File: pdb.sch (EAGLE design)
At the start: 38 parts, among them Q1 20MHz, Q2 IRFR5305PBF, Q3 IRFR5305PBF, U1 TSR_1-2433, U2 LTC2946CMSPBF, U3 LTC2946CMSPBF, U4 LTC2946CMSPBF, U5 ATMEGA48-20AU, U6 TXB0104, U7 AT30TS74SS8M

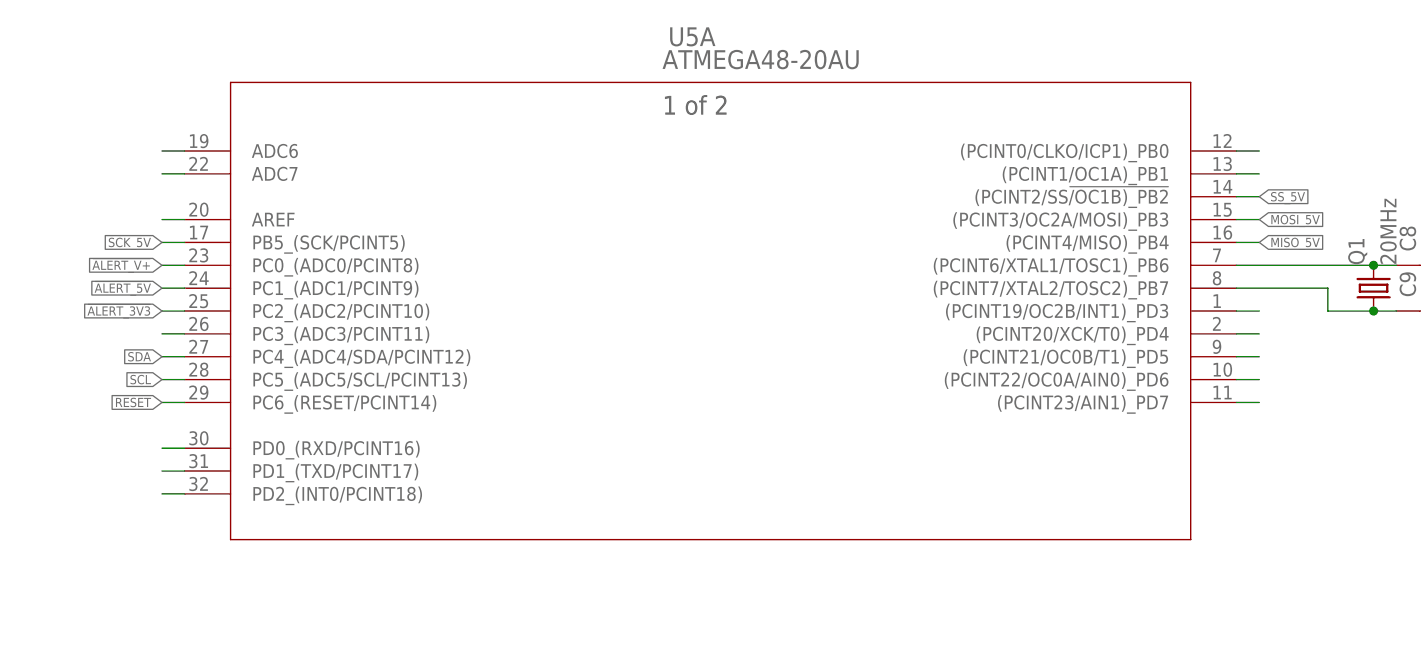
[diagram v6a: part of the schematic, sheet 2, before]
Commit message: 5v nearly completely connected
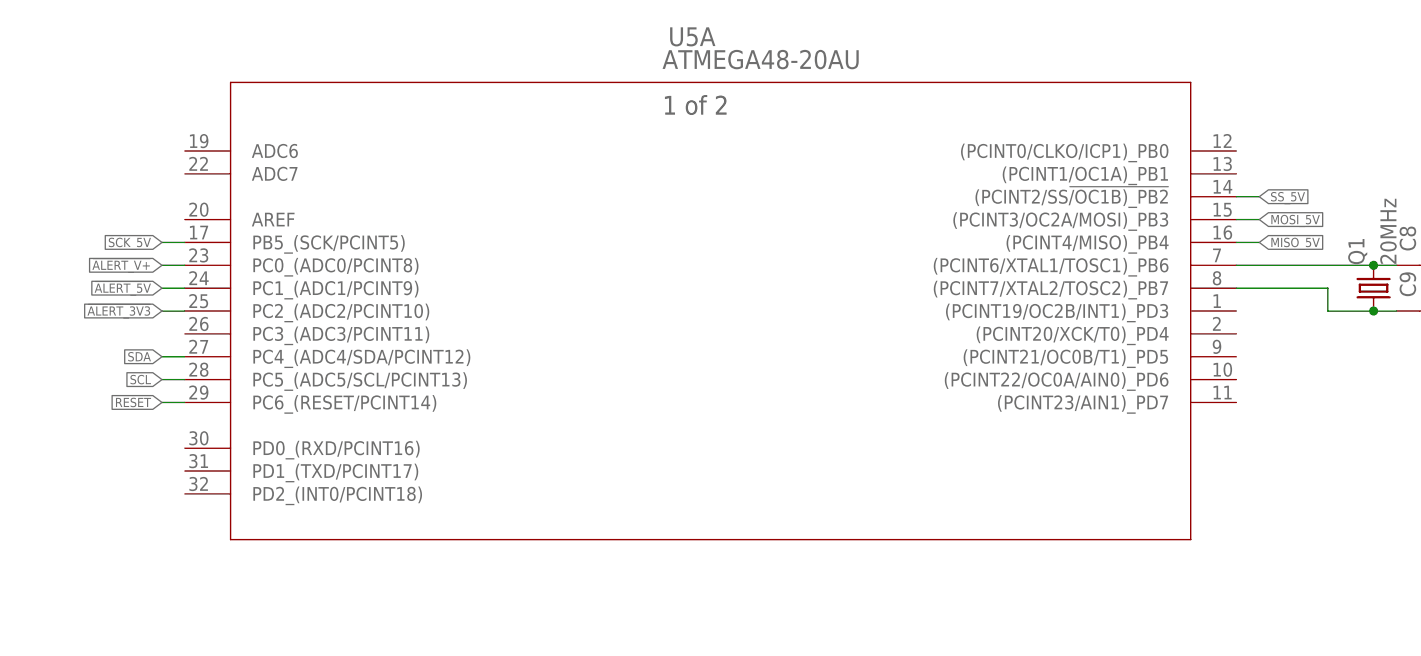
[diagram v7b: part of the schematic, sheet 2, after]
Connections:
- removed net ADIN_3V3: U4.ADIN
- removed net ADIN_5V: U3.ADIN
- removed net ADIN_V+: U2.ADIN
- removed net CLKIN_3V3: U4.CLKIN
- removed net CLKIN_5V: U3.CLKIN
- removed net CLKIN_V+: U2.CLKIN
- removed net CLKOUT_3V3: U4.CLKOUT
- removed net CLKOUT_5V: U3.CLKOUT
- removed net CLKOUT_V+: U2.CLKOUT
- removed net N$10: U5A.AREF
- removed net N$11: U7.ALERT
- removed net N$13: U7.A2
- removed net N$14: U7.A1
- removed net N$15: U5A.PC3_(ADC3/PCINT11)
- removed net N$16: U7.A0
- removed net N$19: U5A.PD0_(RXD/PCINT16)
- removed net N$20: U5A.PD1_(TXD/PCINT17)
- removed net N$21: U5A.PD2_(INT0/PCINT18)
- removed net N$22: U5A.(PCINT0/CLKO/ICP1)_PB0
- removed net N$23: U5A.(PCINT1/OC1A)_PB1
- removed net N$29: U5A.(PCINT19/OC2B/INT1)_PD3
- removed net N$30: U5A.(PCINT20/XCK/T0)_PD4
- removed net N$31: U5A.(PCINT21/OC0B/T1)_PD5
- removed net N$32: U5A.(PCINT22/OC0A/AIN0)_PD6
- removed net N$33: U5A.(PCINT23/AIN1)_PD7
- removed net N$8: U5A.ADC6
- removed net N$9: U5A.ADC7
- removed net SCL_5V: U7.SCL
- removed net SDA_5V: U7.SDA
- net N$88: now also U5B.AVCC
- net SCL: now also U7.SCL
- net SDA: now also U7.SDA
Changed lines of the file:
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@@
 <clearance class="0" value="0.106"/>
 </class>
-<class number="2" name="+14V" width="1.27" drill="0">
+<class number="2" name="V+" width="1.27" drill="0">
 <clearance class="0" value="0.254"/>
 <clearance class="1" value="0.254"/>
 </class>
-<class number="3" name="GND" width="0.4064" drill="0">
+<class number="3" name="GND" width="0.254" drill="0">
 <clearance class="2" value="0.254"/>
 </class>
@@
 </segment>
 </net>
-<net name="N$8" class="0">
-<segment>
-<pinref part="U5" gate="A" pin="ADC6"/>
-<wire x1="83.82" y1="160.02" x2="81.28" y2="160.02" width="0.1524" layer="91"/>
-</segment>
-</net>
-<net name="N$9" class="0">
-<segment>
-<pinref part="U5" gate="A" pin="ADC7"/>
-<wire x1="83.82" y1="157.48" x2="81.28" y2="157.48" width="0.1524" layer="91"/>
-</segment>
-</net>
-<net name="N$10" class="0">
-<segment>
-<pinref part="U5" gate="A" pin="AREF"/>
-<wire x1="83.82" y1="152.4" x2="81.28" y2="152.4" width="0.1524" layer="91"/>
-</segment>
-</net>
 <net name="SCK_5V" class="0">
 <segment>
@@
 </segment>
 </net>
-<net name="N$15" class="0">
-<segment>
-<pinref part="U5" gate="A" pin="PC3_(ADC3/PCINT11)"/>
-<wire x1="83.82" y1="139.7" x2="81.28" y2="139.7" width="0.1524" layer="91"/>
-</segment>
-</net>
 <net name="SDA" class="0">
 <segment>
@@
 <wire x1="83.82" y1="132.08" x2="81.28" y2="132.08" width="0.1524" layer="91"/>
 <label x="81.28" y="132.08" size="1.016" layer="95" rot="R180" xref="yes"/>
-</segment>
-</net>
-<net name="N$19" class="0">
-<segment>
-<pinref part="U5" gate="A" pin="PD0_(RXD/PCINT16)"/>
-<wire x1="83.82" y1="127" x2="81.28" y2="127" width="0.1524" layer="91"/>
-</segment>
-</net>
-<net name="N$20" class="0">
-<segment>
-<pinref part="U5" gate="A" pin="PD1_(TXD/PCINT17)"/>
-<wire x1="83.82" y1="124.46" x2="81.28" y2="124.46" width="0.1524" layer="91"/>
-</segment>
-</net>
-<net name="N$21" class="0">
-<segment>
-<pinref part="U5" gate="A" pin="PD2_(INT0/PCINT18)"/>
-<wire x1="83.82" y1="121.92" x2="81.28" y2="121.92" width="0.1524" layer="91"/>
-</segment>
-</net>
-<net name="N$22" class="0">
-<segment>
-<pinref part="U5" gate="A" pin="(PCINT0/CLKO/ICP1)_PB0"/>
-<wire x1="200.66" y1="160.02" x2="203.2" y2="160.02" width="0.1524" layer="91"/>
-</segment>
-</net>
-<net name="N$23" class="0">
-<segment>
-<pinref part="U5" gate="A" pin="(PCINT1/OC1A)_PB1"/>
-<wire x1="200.66" y1="157.48" x2="203.2" y2="157.48" width="0.1524" layer="91"/>
 </segment>
 </net>
@@
 </segment>
 </net>
-<net name="N$29" class="0">
-<segment>
-<pinref part="U5" gate="A" pin="(PCINT19/OC2B/INT1)_PD3"/>
-<wire x1="200.66" y1="142.24" x2="203.2" y2="142.24" width="0.1524" layer="91"/>
-</segment>
-</net>
-<net name="N$30" class="0">
-<segment>
-<pinref part="U5" gate="A" pin="(PCINT20/XCK/T0)_PD4"/>
-<wire x1="200.66" y1="139.7" x2="203.2" y2="139.7" width="0.1524" layer="91"/>
-</segment>
-</net>
-<net name="N$31" class="0">
-<segment>
-<pinref part="U5" gate="A" pin="(PCINT21/OC0B/T1)_PD5"/>
-<wire x1="200.66" y1="137.16" x2="203.2" y2="137.16" width="0.1524" layer="91"/>
-</segment>
-</net>
-<net name="N$32" class="0">
-<segment>
-<pinref part="U5" gate="A" pin="(PCINT22/OC0A/AIN0)_PD6"/>
-<wire x1="200.66" y1="134.62" x2="203.2" y2="134.62" width="0.1524" layer="91"/>
-</segment>
-</net>
-<net name="N$33" class="0">
-<segment>
-<pinref part="U5" gate="A" pin="(PCINT23/AIN1)_PD7"/>
-<wire x1="200.66" y1="132.08" x2="203.2" y2="132.08" width="0.1524" layer="91"/>
-</segment>
-</net>
 <net name="N$88" class="0">
 <segment>
@@
 <wire x1="106.68" y1="55.88" x2="106.68" y2="50.8" width="0.1524" layer="91"/>
 <junction x="93.98" y="55.88"/>
+<pinref part="U5" gate="B" pin="AVCC"/>
 </segment>
 </net>
@@
 </segment>
 </net>
-<net name="CLKIN_V+" class="0">
-<segment>
-<pinref part="U2" gate="A" pin="CLKIN"/>
-<wire x1="38.1" y1="86.36" x2="35.56" y2="86.36" width="0.1524" layer="91"/>
-</segment>
-</net>
-<net name="ADIN_V+" class="0">
-<segment>
-<pinref part="U2" gate="A" pin="ADIN"/>
-<wire x1="38.1" y1="99.06" x2="35.56" y2="99.06" width="0.1524" layer="91"/>
-</segment>
-</net>
 <net name="INTVCC_V+" class="0">
 <segment>
@@
 </segment>
 </net>
-<net name="CLKOUT_V+" class="0">
-<segment>
-<pinref part="U2" gate="A" pin="CLKOUT"/>
-<wire x1="83.82" y1="99.06" x2="86.36" y2="99.06" width="0.1524" layer="91"/>
-</segment>
-</net>
 <net name="GPIO1_V+" class="0">
 <segment>
@@
 <wire x1="134.62" y1="76.2" x2="132.08" y2="76.2" width="0.1524" layer="91"/>
 <label x="132.08" y="76.2" size="1.016" layer="95" rot="R180" xref="yes"/>
-</segment>
-</net>
-<net name="CLKIN_5V" class="0">
-<segment>
-<pinref part="U3" gate="A" pin="CLKIN"/>
-<wire x1="134.62" y1="86.36" x2="132.08" y2="86.36" width="0.1524" layer="91"/>
-</segment>
-</net>
-<net name="ADIN_5V" class="0">
-<segment>
-<pinref part="U3" gate="A" pin="ADIN"/>
-<wire x1="134.62" y1="99.06" x2="132.08" y2="99.06" width="0.1524" layer="91"/>
-</segment>
-</net>
-<net name="CLKOUT_5V" class="0">
-<segment>
-<pinref part="U3" gate="A" pin="CLKOUT"/>
-<wire x1="180.34" y1="99.06" x2="182.88" y2="99.06" width="0.1524" layer="91"/>
 </segment>
 </net>
@@
 <wire x1="251.46" y1="76.2" x2="248.92" y2="76.2" width="0.1524" layer="91"/>
 <label x="248.92" y="76.2" size="1.016" layer="95" rot="R180" xref="yes"/>
-</segment>
-</net>
-<net name="CLKIN_3V3" class="0">
-<segment>
-<pinref part="U4" gate="A" pin="CLKIN"/>
-<wire x1="251.46" y1="86.36" x2="248.92" y2="86.36" width="0.1524" layer="91"/>
-</segment>
-</net>
-<net name="ADIN_3V3" class="0">
-<segment>
-<pinref part="U4" gate="A" pin="ADIN"/>
-<wire x1="251.46" y1="99.06" x2="248.92" y2="99.06" width="0.1524" layer="91"/>
-</segment>
-</net>
-<net name="CLKOUT_3V3" class="0">
-<segment>
-<pinref part="U4" gate="A" pin="CLKOUT"/>
-<wire x1="297.18" y1="99.06" x2="299.72" y2="99.06" width="0.1524" layer="91"/>
 </segment>
 </net>
@@
 </busses>
 <nets>
-<net name="SDA_5V" class="0">
+<net name="SDA" class="0">
 <segment>
 <pinref part="U7" gate="IC1" pin="SDA"/>
@@
 </segment>
 </net>
-<net name="SCL_5V" class="0">
+<net name="SCL" class="0">
 <segment>
 <pinref part="U7" gate="IC1" pin="SCL"/>
@@
 </segment>
 </net>
-<net name="N$11" class="0">
-<segment>
-<pinref part="U7" gate="IC1" pin="ALERT"/>
-<wire x1="109.22" y1="139.7" x2="106.68" y2="139.7" width="0.1524" layer="91"/>
-</segment>
-</net>
-<net name="N$13" class="0">
-<segment>
-<pinref part="U7" gate="IC1" pin="A2"/>
-<wire x1="139.7" y1="134.62" x2="142.24" y2="134.62" width="0.1524" layer="91"/>
-</segment>
-</net>
-<net name="N$14" class="0">
-<segment>
-<pinref part="U7" gate="IC1" pin="A1"/>
-<wire x1="139.7" y1="139.7" x2="142.24" y2="139.7" width="0.1524" layer="91"/>
-</segment>
-</net>
-<net name="N$16" class="0">
-<segment>
-<pinref part="U7" gate="IC1" pin="A0"/>
-<wire x1="139.7" y1="144.78" x2="142.24" y2="144.78" width="0.1524" layer="91"/>
-</segment>
-</net>

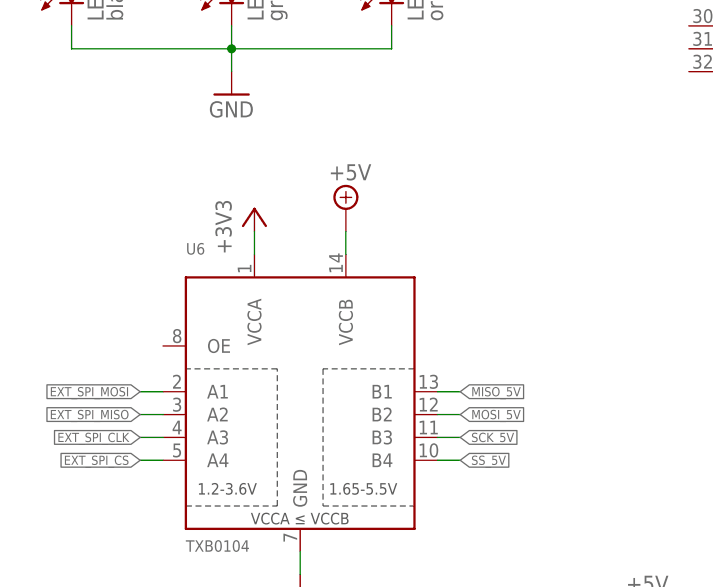
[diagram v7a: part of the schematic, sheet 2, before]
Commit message: fixed spi level shifting
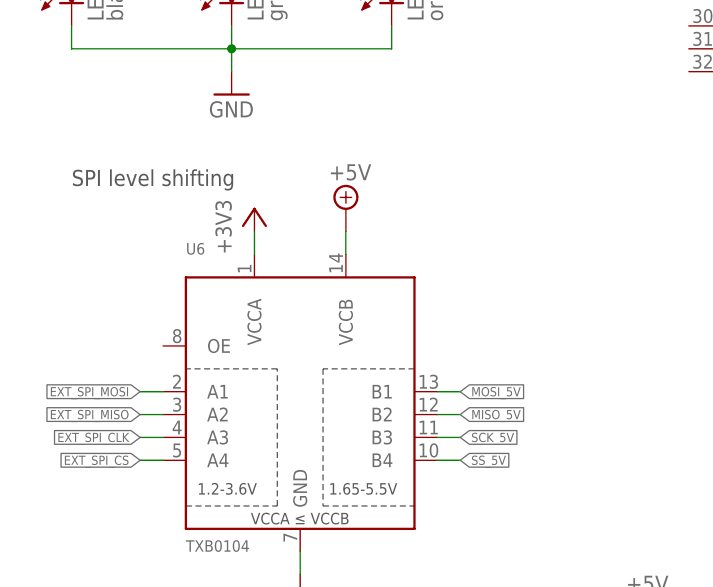
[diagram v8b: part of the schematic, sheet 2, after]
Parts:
- renumbered U$2 to BAT
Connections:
- net MISO_5V: now also U6.B2; no longer U6.B1
- net MOSI_5V: now also U6.B1; no longer U6.B2
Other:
- note added: "SPI level shifting"
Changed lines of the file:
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@@
 <?xml version="1.0" encoding="utf-8"?>
 <!DOCTYPE eagle SYSTEM "eagle.dtd">
-<eagle version="8.5.1">
+<eagle version="8.5.2">
 <drawing>
 <settings>
-<setting alwaysvectorfont="no"/>
+<setting alwaysvectorfont="yes"/>
 <setting verticaltext="up"/>
 </settings>
@@
 <part name="U1" library="Robo-Lib" deviceset="TSR_1-*" device="" technology="2433"/>
 <part name="SUPPLY6" library="supply2" library_urn="urn:adsk.eagle:library:372" deviceset="V+" device=""/>
-<part name="U$2" library="amass" deviceset="XT60PW" device="MALE"/>
+<part name="BAT" library="amass" deviceset="XT60PW" device="MALE"/>
 <part name="LED1" library="led" library_urn="urn:adsk.eagle:library:259" deviceset="LED" device="CHIP-LED0603" package3d_urn="urn:adsk.eagle:package:15819/3" value="blau"/>
 <part name="LED2" library="led" library_urn="urn:adsk.eagle:library:259" deviceset="LED" device="CHIP-LED0603" package3d_urn="urn:adsk.eagle:package:15819/3" value="grün"/>
@@
 <instance part="U1" gate="G$1" x="2.54" y="15.24"/>
 <instance part="SUPPLY6" gate="1" x="-12.7" y="20.32"/>
-<instance part="U$2" gate="G$1" x="-99.06" y="53.34" rot="MR0"/>
+<instance part="BAT" gate="G$1" x="-99.06" y="53.34" rot="MR0"/>
 <instance part="R4" gate="G$1" x="-27.94" y="55.88"/>
 <instance part="R5" gate="G$1" x="25.4" y="55.88"/>
@@
 <wire x1="-81.28" y1="50.8" x2="-81.28" y2="48.26" width="0.1524" layer="91"/>
 <pinref part="GND25" gate="1" pin="GND"/>
-<pinref part="U$2" gate="G$1" pin="-"/>
+<pinref part="BAT" gate="G$1" pin="-"/>
 </segment>
 <segment>
@@
 <pinref part="Q2" gate="G$1" pin="D"/>
 <wire x1="-88.9" y1="55.88" x2="-78.74" y2="55.88" width="0.1524" layer="91"/>
-<pinref part="U$2" gate="G$1" pin="+"/>
+<pinref part="BAT" gate="G$1" pin="+"/>
 </segment>
 </net>
@@
 <plain>
 <text x="15.24" y="165.1" size="1.778" layer="97">Powerleds</text>
+<text x="15.24" y="109.22" size="1.778" layer="97">SPI level shifting</text>
 </plain>
 <instances>
@@
 </segment>
 <segment>
+<pinref part="U6" gate="G$1" pin="B1"/>
+<wire x1="55.88" y1="86.36" x2="58.42" y2="86.36" width="0.1524" layer="91"/>
+<label x="58.42" y="86.36" size="1.016" layer="95" xref="yes"/>
+</segment>
+</net>
+<net name="MISO_5V" class="0">
+<segment>
+<pinref part="U5" gate="A" pin="(PCINT4/MISO)_PB4"/>
+<wire x1="200.66" y1="149.86" x2="203.2" y2="149.86" width="0.1524" layer="91"/>
+<label x="203.2" y="149.86" size="1.016" layer="95" xref="yes"/>
+</segment>
+<segment>
 <pinref part="U6" gate="G$1" pin="B2"/>
 <wire x1="55.88" y1="83.82" x2="58.42" y2="83.82" width="0.1524" layer="91"/>
@@
 </segment>
 </net>
-<net name="MISO_5V" class="0">
-<segment>
-<pinref part="U5" gate="A" pin="(PCINT4/MISO)_PB4"/>
-<wire x1="200.66" y1="149.86" x2="203.2" y2="149.86" width="0.1524" layer="91"/>
-<label x="203.2" y="149.86" size="1.016" layer="95" xref="yes"/>
-</segment>
-<segment>
-<pinref part="U6" gate="G$1" pin="B1"/>
-<wire x1="55.88" y1="86.36" x2="58.42" y2="86.36" width="0.1524" layer="91"/>
-<label x="58.42" y="86.36" size="1.016" layer="95" xref="yes"/>
-</segment>
-</net>
